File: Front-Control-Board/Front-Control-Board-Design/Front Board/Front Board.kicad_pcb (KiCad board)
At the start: 2 copper layers, 4 parts, among them U1 ESP32-WROOM-32, U2 NCP1117-5.0_TO252

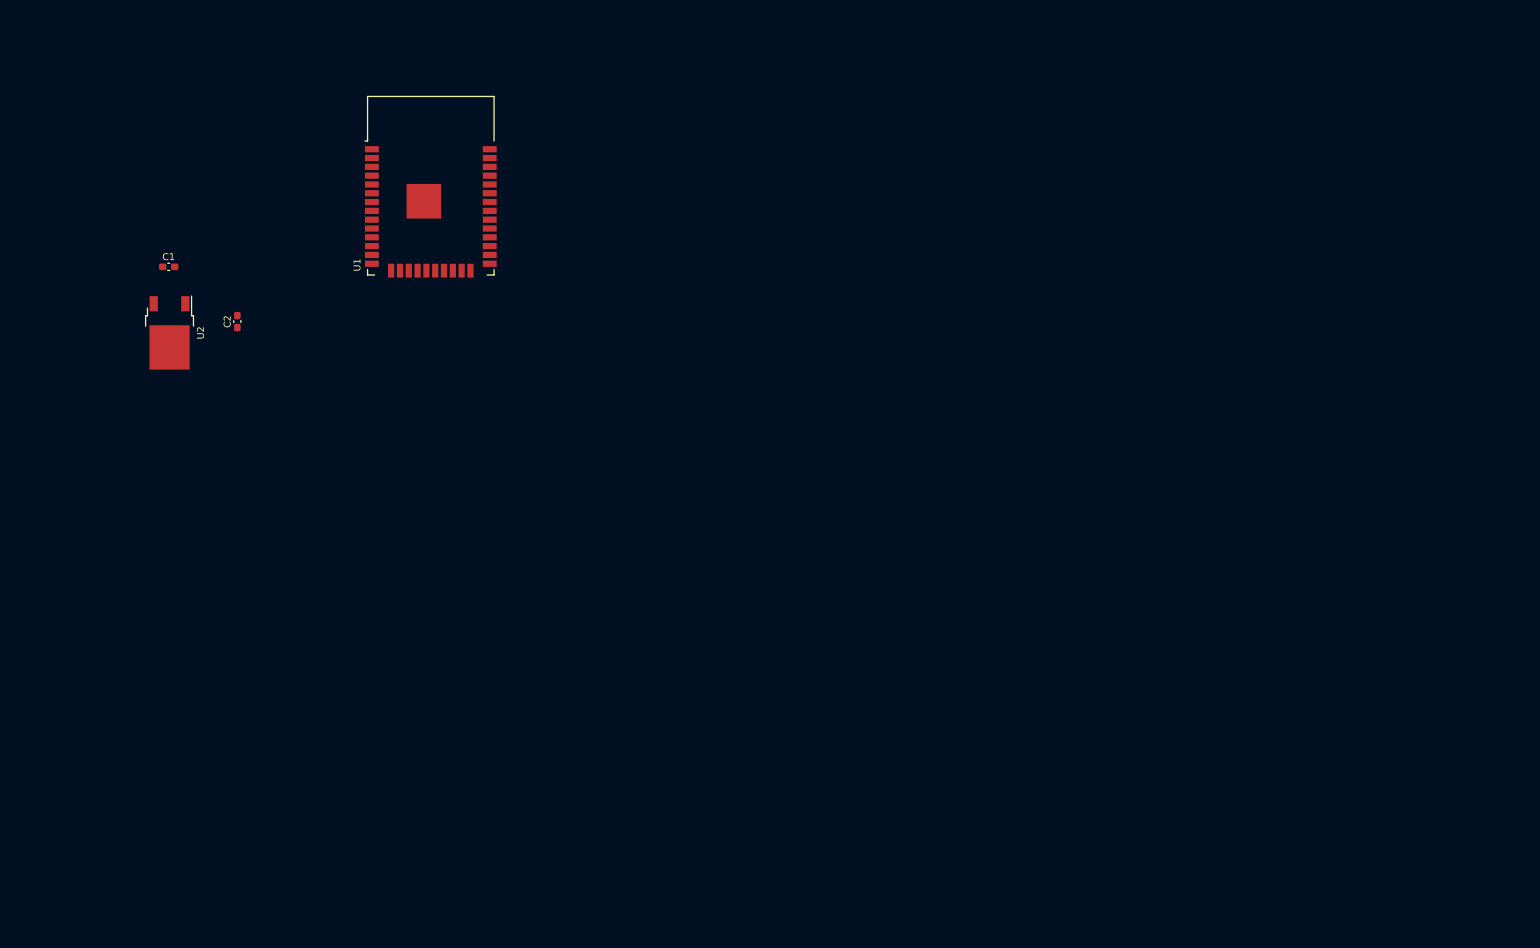
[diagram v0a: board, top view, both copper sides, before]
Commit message: Front board schematic
and linking to footprint done
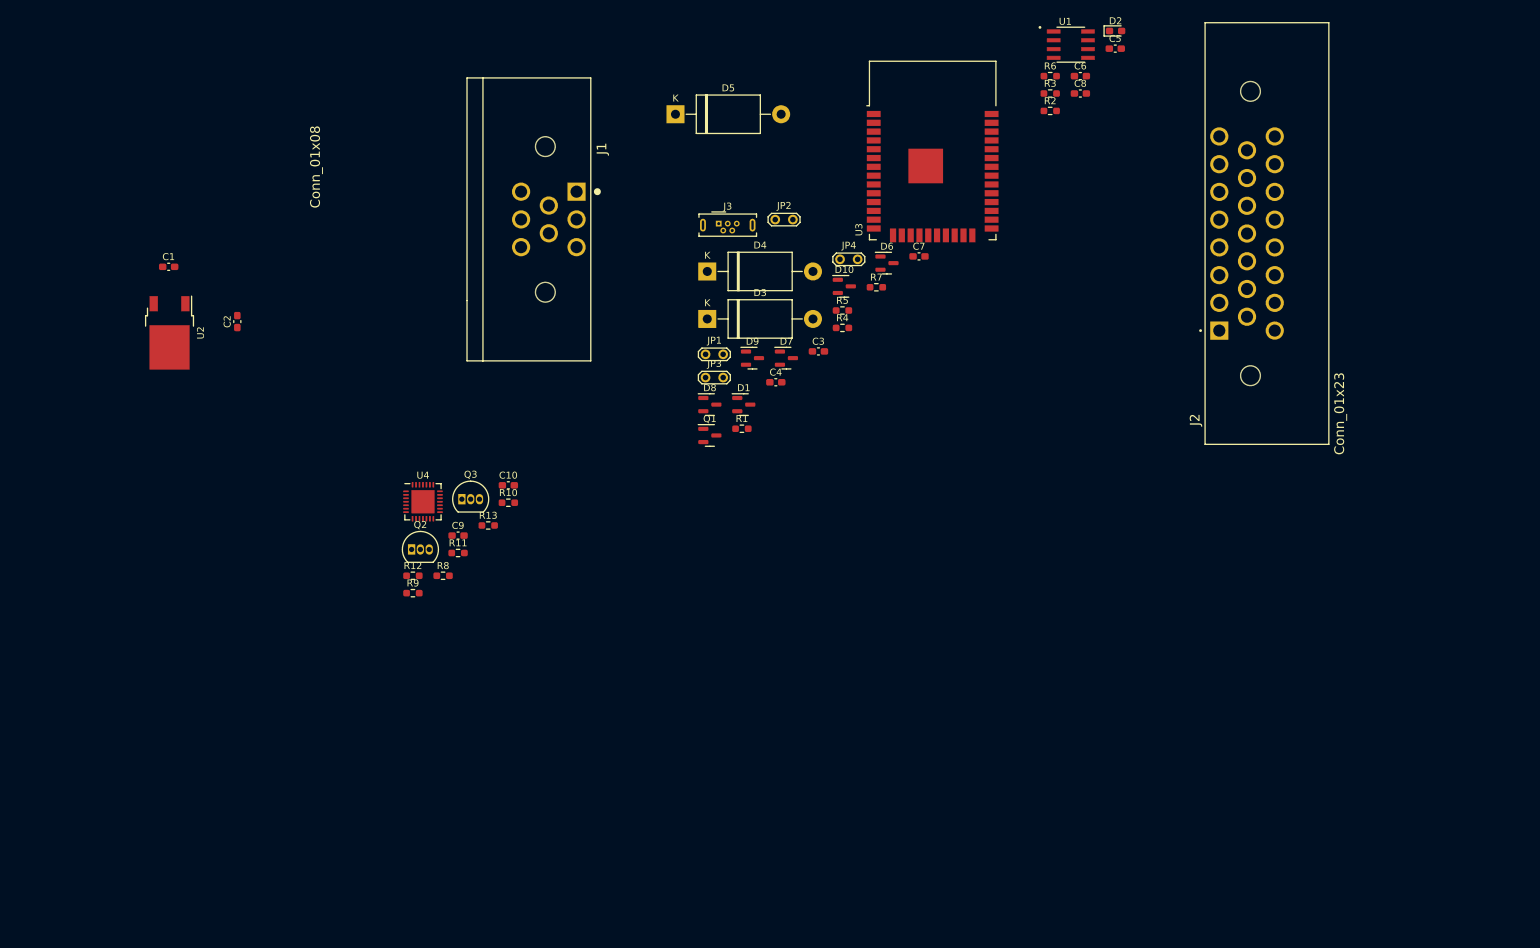
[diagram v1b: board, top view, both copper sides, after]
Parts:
- added C10: 0.1uF, Capacitor_SMD:C_0603_1608Metric_Pad1.08x0.95mm_HandSolder, F.Cu at (118.9, 106.0)
- added C3: 0.1u, Capacitor_SMD:C_0603_1608Metric_Pad1.08x0.95mm_HandSolder, F.Cu at (163.6, 86.7)
- added C4: 0.1u, Capacitor_SMD:C_0603_1608Metric_Pad1.08x0.95mm_HandSolder, F.Cu at (157.4, 91.2)
- added C5: 0.1u, Capacitor_SMD:C_0603_1608Metric_Pad1.08x0.95mm_HandSolder, F.Cu at (206.4, 43.0)
- added C6: 0.1f, Capacitor_SMD:C_0603_1608Metric_Pad1.08x0.95mm_HandSolder, F.Cu at (201.4, 47.0)
- added C7: 0.1f, Capacitor_SMD:C_0603_1608Metric_Pad1.08x0.95mm_HandSolder, F.Cu at (178.1, 73.0)
- added C8: 0.1f, Capacitor_SMD:C_0603_1608Metric_Pad1.08x0.95mm_HandSolder, F.Cu at (201.4, 49.5)
- added C9: 4.7uF, Capacitor_SMD:C_0603_1608Metric_Pad1.08x0.95mm_HandSolder, F.Cu at (111.6, 113.3)
- added D1: DESD2CAN2SOQ-7, Package_TO_SOT_SMD:SOT-23, F.Cu at (152.8, 94.4)
- added D10: SP0502BAHT, Package_TO_SOT_SMD:SOT-23, F.Cu at (167.3, 77.3)
- added D2: LED, LED_SMD:LED_0603_1608Metric_Pad1.05x0.95mm_HandSolder, F.Cu at (206.4, 40.5)
- added D3: 1N630xCA, Diode_THT:D_DO-201AE_P15.24mm_Horizontal, F.Cu at (147.6, 82.0)
- added D4: 1N630xCA, Diode_THT:D_DO-201AE_P15.24mm_Horizontal, F.Cu at (147.6, 75.2)
- added D5: 1N630xCA, Diode_THT:D_DO-201AE_P15.24mm_Horizontal, F.Cu at (143.0, 52.5)
- added D6: SP0502BAHT, Package_TO_SOT_SMD:SOT-23, F.Cu at (173.5, 74.0)
- added D7: SP0502BAHT, Package_TO_SOT_SMD:SOT-23, F.Cu at (159.0, 87.7)
- added D8: SP0502BAHT, Package_TO_SOT_SMD:SOT-23, F.Cu at (147.9, 94.4)
- added D9: SP0502BAHT, Package_TO_SOT_SMD:SOT-23, F.Cu at (154.1, 87.7)
- added J1: Conn_01x08, AERO_Footprints:TE_1-776280-1_8pin_Horizontal, F.Cu at (124.2, 67.7)
- added J2: Conn_01x23, AERO_Footprints:TE_1-770669-1_23pin_Horizontal, F.Cu at (221.4, 83.7)
- added J3: USB_B_Micro, Connector_USB:USB_Micro-B_Wuerth_614105150721_Vertical, F.Cu at (149.2, 68.3)
- added JP1: JOpen, TestPoint:TestPoint_2Pads_Pitch2.54mm_Drill0.8mm, F.Cu at (147.3, 87.1)
- added JP2: JOpen, TestPoint:TestPoint_2Pads_Pitch2.54mm_Drill0.8mm, F.Cu at (157.4, 67.7)
- added JP3: JOpen, TestPoint:TestPoint_2Pads_Pitch2.54mm_Drill0.8mm, F.Cu at (147.3, 90.5)
- added JP4: JOpen, TestPoint:TestPoint_2Pads_Pitch2.54mm_Drill0.8mm, F.Cu at (166.7, 73.4)
- added Q1: 2N7002, Package_TO_SOT_SMD:SOT-23, F.Cu at (147.9, 98.8)
- added Q2: S8050, Package_TO_SOT_THT:TO-92_Inline, F.Cu at (104.9, 115.3)
- added Q3: S8050, Package_TO_SOT_THT:TO-92_Inline, F.Cu at (112.2, 108.0)
- added R1: 120, Resistor_SMD:R_0603_1608Metric_Pad0.98x0.95mm_HandSolder, F.Cu at (152.6, 97.8)
- added R10: 22.1k, Resistor_SMD:R_0603_1608Metric_Pad0.98x0.95mm_HandSolder, F.Cu at (118.9, 108.5)
- added R11: 47.5k, Resistor_SMD:R_0603_1608Metric_Pad0.98x0.95mm_HandSolder, F.Cu at (111.6, 115.8)
- added R12: 10k, Resistor_SMD:R_0603_1608Metric_Pad0.98x0.95mm_HandSolder, F.Cu at (105.1, 119.0)
- added R13: 10K, Resistor_SMD:R_0603_1608Metric_Pad0.98x0.95mm_HandSolder, F.Cu at (116.0, 111.8)
- added R2: 330, Resistor_SMD:R_0603_1608Metric_Pad0.98x0.95mm_HandSolder, F.Cu at (197.0, 52.0)
- added R3: 10k, Resistor_SMD:R_0603_1608Metric_Pad0.98x0.95mm_HandSolder, F.Cu at (197.0, 49.5)
- added R4: 100, Resistor_SMD:R_0603_1608Metric_Pad0.98x0.95mm_HandSolder, F.Cu at (167.1, 83.3)
- added R5: 100, Resistor_SMD:R_0603_1608Metric_Pad0.98x0.95mm_HandSolder, F.Cu at (167.1, 80.8)
- added R6: 10k, Resistor_SMD:R_0603_1608Metric_Pad0.98x0.95mm_HandSolder, F.Cu at (197.0, 47.0)
- added R7: 100, Resistor_SMD:R_0603_1608Metric_Pad0.98x0.95mm_HandSolder, F.Cu at (171.9, 77.5)
- added R8: 2k, Resistor_SMD:R_0603_1608Metric_Pad0.98x0.95mm_HandSolder, F.Cu at (109.5, 119.0)
- added R9: 10K, Resistor_SMD:R_0603_1608Metric_Pad0.98x0.95mm_HandSolder, F.Cu at (105.1, 121.6)
- added U3: ESP32-WROOM-32D, RF_Module:ESP32-WROOM-32, F.Cu at (180.1, 60.7)
- added U4: CP2102N-Axx-xQFN28, Package_DFN_QFN:QFN-28-1EP_5x5mm_P0.5mm_EP3.35x3.35mm, F.Cu at (106.6, 108.4)
- U1: value ESP32-WROOM-32 -> MAX33054EASA+T; footprint RF_Module:ESP32-WROOM-32 -> AERO_Footprints:SOIC127P600X175-8N
- moved U1 95.2 mm to (200.0, 42.5)
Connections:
- C2 pad 1: VDD -> EN
- U1 pad 1: GND -> /CAN_TX
- U1 pad 2: VDD -> GND
- U1 pad 3: VDD -> +3V3
- U1 pad 4: unconnected-(U1-Pad4) -> /CAN_RX
- U1 pad 5: unconnected-(U1-Pad5) -> +3V3
- U1 pad 6: unconnected-(U1-Pad6) -> /CAN_N
- U1 pad 7: unconnected-(U1-Pad7) -> /CAN_P
- U1 pad 8: unconnected-(U1-Pad8) -> GND
- U2 pad 2: VDD -> EN

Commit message: front board with footprint
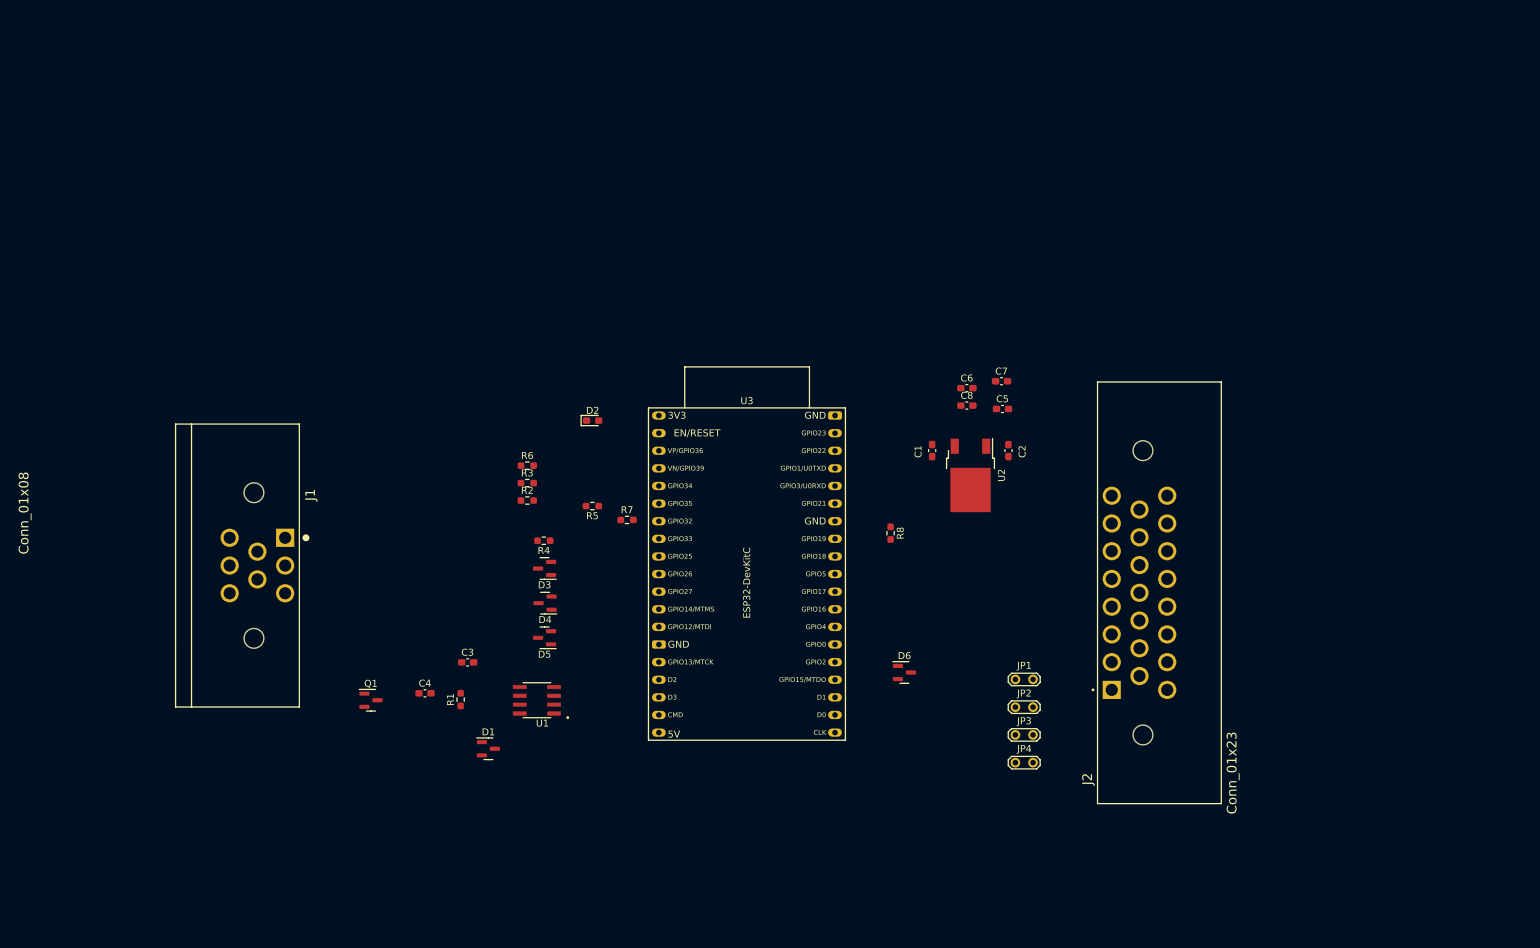
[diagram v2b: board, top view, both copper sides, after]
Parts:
- removed C10: 0.1uF, Capacitor_SMD:C_0603_1608Metric_Pad1.08x0.95mm_HandSolder
- removed C9: 4.7uF, Capacitor_SMD:C_0603_1608Metric_Pad1.08x0.95mm_HandSolder
- removed D10, D7, D8, D9: SP0502BAHT, Package_TO_SOT_SMD:SOT-23
- removed J3: USB_B_Micro, Connector_USB:USB_Micro-B_Wuerth_614105150721_Vertical
- removed Q2, Q3: S8050, Package_TO_SOT_THT:TO-92_Inline
- removed R10: 22.1k, Resistor_SMD:R_0603_1608Metric_Pad0.98x0.95mm_HandSolder
- removed R11: 47.5k, Resistor_SMD:R_0603_1608Metric_Pad0.98x0.95mm_HandSolder
- removed R12: 10k, Resistor_SMD:R_0603_1608Metric_Pad0.98x0.95mm_HandSolder
- removed R13, R9: 10K, Resistor_SMD:R_0603_1608Metric_Pad0.98x0.95mm_HandSolder
- removed U4: CP2102N-Axx-xQFN28, Package_DFN_QFN:QFN-28-1EP_5x5mm_P0.5mm_EP3.35x3.35mm
- D3, D4, D5: value 1N630xCA -> SP0502BAHT; footprint Diode_THT:D_DO-201AE_P15.24mm_Horizontal -> Package_TO_SOT_SMD:SOT-23
- R4: value 100 -> 10k
- R6: value 10k -> 100
- R8: value 2k -> 10k
- U3: value ESP32-WROOM-32D -> ESP32-DevKitC; footprint RF_Module:ESP32-WROOM-32 -> Espressif:ESP32-DevKitC
- moved U1 121.9 mm to (123.0, 137.0), turned to 180 degrees
- moved U2 117.3 mm to (185.5, 104.6)
- moved C1 113.2 mm to (180.0, 101.0), turned to -90 degrees
- moved C2 112.7 mm to (191.0, 101.0)
- moved R3 94.0 mm to (121.6, 105.7)
- moved R6 94.0 mm to (121.6, 103.2)
- moved D2 94.0 mm to (131.0, 96.7)
- moved R2 94.0 mm to (121.6, 108.2)
- moved JP2 78.4 mm to (192.0, 138.0)
- moved D5 77.8 mm to (124.1, 128.0), turned to 180 degrees
- moved JP4 76.9 mm to (192.0, 146.0)
- moved JP3 68.2 mm to (192.0, 142.0)
- moved C3 67.6 mm to (113.0, 131.6)
- moved C4 67.6 mm to (106.9, 136.0)
- moved J1 65.2 mm to (82.2, 117.6)
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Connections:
- C2 pad 1: EN -> VDD
- C5 pad 1: EN -> VDD
- C6 pad 1: EN -> VDD
- C7 pad 1: EN -> VDD
- C8 pad 1: EN -> VDD
- D3 pad 1: GND -> /pedal_1
- D3 pad 2: VBUS -> /stearing
- D4 pad 1: D+ -> /R_wheel
- D4 pad 2: GND -> /L_wheel
- D5 pad 1: D- -> /R_sus
- D5 pad 2: GND -> /L_sus
- D6 pad 2: unconnected-(D6-Pad2) -> /Brake_1
- J2 pad 14: EN -> VDD
- J2 pad 16: EN -> VDD
- J2 pad 6: EN -> VDD
- J2 pad 8: EN -> VDD
- JP1 pad 1: EN -> VDD
- JP3 pad 1: EN -> VDD
- R2 pad 1: EN -> VDD
- R4 pad 1: Net-(R4-Pad1) -> /RTD_bttn
- R4 pad 2: /RTD_led -> VDD
- R5 pad 2: /AMS_Led -> /IMD_led
- R6 pad 1: /RTD_bttn -> Net-(R6-Pad1)
- R6 pad 2: EN -> /AMS_Led
- R7 pad 1: unconnected-(R7-Pad1) -> Net-(R7-Pad1)
- R7 pad 2: /IMD_led -> /RTD_led
- R8 pad 1: EN -> GND
- R8 pad 2: Net-(R8-Pad2) -> /LORA Reset
- U2 pad 2: EN -> VDD
- U3 pad 1: GND -> VDD
- U3 pad 10: /stearing -> /pedal_1
- U3 pad 11: /pedal_1 -> /L_wheel
- U3 pad 12: /L_wheel -> /R_wheel
- U3 pad 13: /R_wheel -> /L_sus
- U3 pad 14: /L_sus -> GND
- U3 pad 15: GND -> /R_sus
- U3 pad 16: /R_sus -> /CAN_RX
- U3 pad 17: /CAN_RX -> /CAN_TX
- U3 pad 18: /CAN_TX -> unconnected-(U3-Pad18)
- U3 pad 19: RTS -> unconnected-(U3-Pad19)
- U3 pad 2: EN -> VDD
- U3 pad 20: CTS -> unconnected-(U3-Pad20)
- U3 pad 25: IO0 -> unconnected-(U3-Pad25)
- U3 pad 3: EN -> unconnected-(U3-Pad3)
- U3 pad 32: unconnected-(U3-Pad32) -> GND
- U3 pad 34: RX -> unconnected-(U3-Pad34)
- U3 pad 35: TX -> unconnected-(U3-Pad35)
- U3 pad 5: unconnected-(U3-Pad5) -> Net-(R6-Pad1)
- U3 pad 7: unconnected-(U3-Pad7) -> Net-(R7-Pad1)
- U3 pad 8: Net-(R4-Pad1) -> /RTD_bttn
- U3 pad 9: /RTD_bttn -> /stearing

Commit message: Update
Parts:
- removed C7, C8: 0.1f, Capacitor_SMD:C_0603_1608Metric_Pad1.08x0.95mm_HandSolder
- moved J2 125.6 mm to (84.1, 105.0), turned to -90 degrees
- moved J1 119.0 mm to (201.2, 116.5), turned to 90 degrees
- moved JP1 101.8 mm to (92.5, 112.5)
- moved JP2 101.8 mm to (92.5, 116.5)
- moved JP3 101.8 mm to (92.5, 120.5)
- moved JP4 101.8 mm to (92.5, 124.5)
- moved R2 60.1 mm to (180.1, 94.5), turned to 180 degrees
- moved C5 53.6 mm to (136.5, 95.0), turned to -90 degrees
- moved D2 44.5 mm to (175.5, 94.5)
- moved C4 17.0 mm to (117.8, 123.0)
- moved Q1 17.0 mm to (110.0, 124.0)
- moved C6 16.1 mm to (169.5, 96.5), turned to 90 degrees
- moved R6 12.7 mm to (134.0, 106.0), turned to 180 degrees
- moved C1 9.60 mm to (189.6, 101.0)
- moved C2 9.51 mm to (183.2, 106.5), turned to 0 degrees
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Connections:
- J1 pad 1: +12V -> unconnected-(J1-Pad1)
- J1 pad 2: /CAN_N -> unconnected-(J1-Pad2)
- J1 pad 3: /CAN_P -> unconnected-(J1-Pad3)
- J1 pad 4: /RTD_ind_out -> /CAN_N
- J1 pad 5: +12V -> /CAN_P
- J1 pad 6: unconnected-(J1-Pad6) -> /RTD_ind_out
- J1 pad 7: unconnected-(J1-Pad7) -> +12V
- J2 pad 18: unconnected-(J2-Pad18) -> /LORA Reset
- J2 pad 19: unconnected-(J2-Pad19) -> /LORA NSS
- J2 pad 20: unconnected-(J2-Pad20) -> /LORA_RX
- J2 pad 21: unconnected-(J2-Pad21) -> /LORA_TX
- J2 pad 22: unconnected-(J2-Pad22) -> /AMS_Led
- J2 pad 23: unconnected-(J2-Pad23) -> /IMD_led
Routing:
- net VDD: track 0.00 -> 59.8 mm
- net +12V: track 0.00 -> 33.7 mm
- net /Brake_0: track 0.00 -> 7.30 mm
- net /Brake_1: track 0.00 -> 7.11 mm
- net /LORA Reset: track 0.00 -> 5.21 mm
- net Net-(D2-Pad2): track 0.00 -> 2.80 mm

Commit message: Colin Push
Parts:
- removed C5: 0.1u, Capacitor_SMD:C_0603_1608Metric_Pad1.08x0.95mm_HandSolder
- removed C6: 0.1f, Capacitor_SMD:C_0603_1608Metric_Pad1.08x0.95mm_HandSolder
- removed JP1, JP2, JP3, JP4: JOpen, TestPoint:TestPoint_2Pads_Pitch2.54mm_Drill0.8mm
- added D7: TS4148C RZG, Diode_SMD:D_0603_1608Metric_Pad1.05x0.95mm_HandSolder, B.Cu at (123.8, 100.1)
- C1, C2, C3, R2: moved to B.Cu
- U2: value NCP1117-5.0_TO252 -> TS2940CP33 ROG; moved to B.Cu
- moved C1 62.1 mm to (128.0, 93.5), turned to 0 degrees
- moved R2 56.3 mm to (123.8, 95.5), turned to -90 degrees
- moved C2 54.8 mm to (128.5, 105.0), turned to 180 degrees
- moved U2 51.2 mm to (130.4, 100.0), turned to 0 degrees
- moved D2 41.0 mm to (134.5, 94.0), turned to 180 degrees
- moved J2 38.4 mm to (122.5, 106.0)
- moved Q1 35.3 mm to (135.9, 100.0), turned to 180 degrees
- moved C3 24.8 mm to (137.5, 135.5), turned to -90 degrees
- moved R3 20.2 mm to (132.5, 100.0), turned to 90 degrees
- moved J1 20.0 mm to (181.2, 117.0)
- moved D1 19.2 mm to (135.0, 141.5)
- moved R1 19.1 mm to (130.5, 141.5)
- moved C4 13.3 mm to (123.5, 135.0), turned to -90 degrees
- moved U1 10.1 mm to (133.0, 135.5)
- moved R4 6.02 mm to (136.1, 114.0)
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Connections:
- J1 pad 1: unconnected-(J1-Pad1) -> GND
- J1 pad 2: unconnected-(J1-Pad2) -> /LORA NSS
- J1 pad 3: unconnected-(J1-Pad3) -> /LORA Reset
- J1 pad 4: /CAN_N -> /LORA_RX
- J1 pad 5: /CAN_P -> /LORA_TX
- J1 pad 6: /RTD_ind_out -> /pedal_0
- J1 pad 7: +12V -> /Brake_0
- J1 pad 8: GND -> /Brake_1
- J2 pad 10: Net-(J2-Pad10) -> VDD
- J2 pad 12: Net-(J2-Pad12) -> VDD
- J2 pad 13: /Brake_0 -> unconnected-(J2-Pad13)
- J2 pad 15: /Brake_1 -> /RTD_ind_out
- J2 pad 16: VDD -> +12V
- J2 pad 18: /LORA Reset -> +12V
- J2 pad 19: /LORA NSS -> /RTD_ind_out
- J2 pad 2: +12V -> VDD
- J2 pad 20: /LORA_RX -> /CAN_N
- J2 pad 21: /LORA_TX -> /CAN_P
- J2 pad 4: +12V -> VDD
- J2 pad 9: /pedal_0 -> unconnected-(J2-Pad9)
- R3 pad 1: unconnected-(R3-Pad1) -> /RTD_ind_sig
- U3 pad 3: unconnected-(U3-Pad3) -> /RTD_ind_sig
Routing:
- net VDD: track 59.8 -> 2.54 mm
- net +12V: track 33.7 -> 0.00 mm
- net /Brake_1: track 7.11 -> 37.6 mm
- net /Brake_0: track 7.30 -> 32.1 mm
- net /pedal_0: track 0.00 -> 20.9 mm
- net /LORA_RX: track 0.00 -> 18.4 mm
- net /LORA_TX: track 0.00 -> 17.5 mm
- net /LORA NSS: track 0.00 -> 11.0 mm
- net /LORA Reset: track 5.21 -> 12.3 mm
- net /CAN_TX: track 0.00 -> 5.68 mm
- net /CAN_RX: track 0.00 -> 5.30 mm
- net Net-(D2-Pad2): track 2.80 -> 0.00 mm
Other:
- board outline added: 77.5 x 53.5 mm

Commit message: Front board first draft
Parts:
- moved D1 10.0 mm to (125.0, 141.5)
- moved C4 8.86 mm to (132.0, 137.5), turned to 180 degrees
- moved R2 6.84 mm to (130.5, 94.0), turned to 0 degrees
- moved U1 6.08 mm to (134.0, 141.5)
- moved C3 6.00 mm to (137.5, 141.5)
- moved C1 3.66 mm to (124.6, 95.0), turned to 180 degrees
- moved R1 1.75 mm to (128.8, 141.5)
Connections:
- C3 pad 1: +3V3 -> VDD
- C4 pad 1: +3V3 -> VDD
- J2 pad 1: /R_wheel -> /RTD_ind_out
- J2 pad 10: VDD -> /RTD_led
- J2 pad 11: /pedal_1 -> /stearing
- J2 pad 12: VDD -> /L_wheel
- J2 pad 13: unconnected-(J2-Pad13) -> /L_sus
- J2 pad 15: /RTD_ind_out -> /CAN_P
- J2 pad 16: +12V -> VDD
- J2 pad 17: /stearing -> VDD
- J2 pad 18: +12V -> VDD
- J2 pad 19: /RTD_ind_out -> VDD
- J2 pad 2: VDD -> /IMD_led
- J2 pad 20: /CAN_N -> VDD
- J2 pad 21: /CAN_P -> VDD
- J2 pad 22: /AMS_Led -> +12V
- J2 pad 23: /IMD_led -> +12V
- J2 pad 3: /L_wheel -> /RTD_bttn
- J2 pad 4: VDD -> /pedal_1
- J2 pad 5: /R_sus -> /R_wheel
- J2 pad 6: VDD -> /R_sus
- J2 pad 7: /L_sus -> unconnected-(J2-Pad7)
- J2 pad 8: VDD -> /CAN_N
- J2 pad 9: unconnected-(J2-Pad9) -> /AMS_Led
- U1 pad 3: +3V3 -> VDD
- U1 pad 5: +3V3 -> VDD
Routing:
- net VDD: track 2.54 -> 125.7 mm, vias 0 -> 3
- net +12V: track 0.00 -> 54.2 mm
- net /L_sus: track 0.00 -> 23.6 mm
- net /L_wheel: track 0.00 -> 23.2 mm
- net /stearing: track 0.00 -> 22.8 mm
- net /R_sus: track 0.00 -> 21.2 mm
- net /CAN_P: track 0.00 -> 20.7 mm
- net /RTD_bttn: track 0.00 -> 19.5 mm
- net /R_wheel: track 0.00 -> 18.9 mm
- net /pedal_1: track 0.00 -> 18.5 mm
- net /AMS_Led: track 0.00 -> 17.4 mm
- net /RTD_led: track 0.00 -> 17.1 mm
- net /CAN_N: track 0.00 -> 16.5 mm
- net /RTD_ind_out: track 0.00 -> 15.0 mm
- net /IMD_led: track 0.00 -> 13.2 mm
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- added copper zone on B.Cu, net GND
- added copper zone on F.Cu, net GND
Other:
- board size 77.5 x 53.5 mm -> 78 x 53.5 mm
